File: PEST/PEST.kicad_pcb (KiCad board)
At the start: 4 copper layers, 6.2 x 4.9 mm, 4 parts, among them J1 Conn_01x01, J2 Conn_01x01, J3 Conn_01x01, J4 Conn_01x01

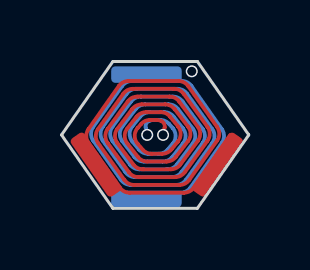
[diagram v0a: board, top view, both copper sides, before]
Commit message: Updated PEST for SMD mounting
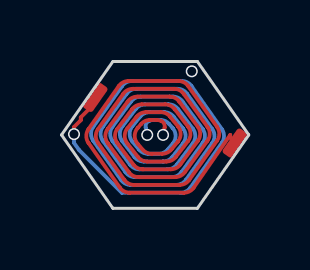
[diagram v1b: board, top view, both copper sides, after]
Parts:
- removed J3, J4: Conn_01x01, PEST:Bridge_Pad
- J2: moved to F.Cu
- moved J2 3.80 mm to (18.0, 18.8), turned to 55 degrees
- moved J1 0.92 mm to (22.7, 20.3)
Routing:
- net Net-(J1-Pin_1): track 195.2 -> 199.7 mm, vias 3 -> 4
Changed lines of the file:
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@@
   (net 1 "Net-(J1-Pin_1)")
   (footprint "PEST:Bridge_Pad" (layer "F.Cu")
-    (at 22.08 20.99 55)
+    (at 22.66 20.27 55)
     (property "Sheetfile" "PEST.kicad_sch")
     (property "Sheetname" "")
@@
         (effects (font (size 1 1) (thickness 0.15)))
     )
-    (fp_text user "${REFERENCE}" (at 0 2.5 55 unlocked) (layer "F.Fab")
-        (effects (font (size 1 1) (thickness 0.15)))
-    )
-    (pad "1" smd roundrect (at 0 0 55) (size 2.35 0.55) (layers "F.Cu" "F.Paste" "F.Mask") (roundrect_rratio 0.25)
+    (pad "1" smd roundrect (at 0 0 55) (size 1 0.4) (layers "F.Cu" "F.Paste" "F.Mask") (roundrect_rratio 0.25)
       (net 1 "Net-(J1-Pin_1)") (pinfunction "Pin_1") (pintype "passive") (thermal_bridge_angle 45))
   )
   (footprint "PEST:Bridge_Pad" (layer "F.Cu")
-    (at 18.03 20.99 -55)
+    (at 18 18.75 55)
     (property "Sheetfile" "PEST.kicad_sch")
     (property "Sheetname" "")
@@
     (property "ki_keywords" "connector")
     (attr smd)
-    (fp_text reference "J3" (at -2.5 -0.5 -55 unlocked) (layer "F.SilkS") hide
+    (fp_text reference "J2" (at -2.5 -0.5 55 unlocked) (layer "F.SilkS") hide
         (effects (font (size 1 1) (thickness 0.1)))
     )
-    (fp_text value "Conn_01x01" (at 0 1 -55 unlocked) (layer "F.Fab")
+    (fp_text value "Conn_01x01" (at 0 1 55 unlocked) (layer "F.Fab")
         (effects (font (size 1 1) (thickness 0.15)))
     )
-    (fp_text user "${REFERENCE}" (at 0 2.5 -55 unlocked) (layer "F.Fab")
+    (fp_text user "${REFERENCE}" (at 0 2.5 55 unlocked) (layer "F.Fab")
         (effects (font (size 1 1) (thickness 0.15)))
     )
-    (pad "1" smd roundrect (at 0 0 305) (size 2.35 0.55) (layers "F.Cu" "F.Paste" "F.Mask") (roundrect_rratio 0.25)
-      (net 1 "Net-(J1-Pin_1)") (pinfunction "Pin_1") (pintype "passive") (thermal_bridge_angle 45))
-  )
-  (footprint "PEST:Bridge_Pad" (layer "B.Cu")
-    (at 19.71 17.99)
-    (property "Sheetfile" "PEST.kicad_sch")
-    (property "Sheetname" "")
-    (property "ki_description" "Generic connector, single row, 01x01, script generated (kicad-library-utils/schlib/autogen/connector/)")
-    (property "ki_keywords" "connector")
-    (attr smd)
-    (fp_text reference "J4" (at -2.5 0.5 180 unlocked) (layer "B.SilkS") hide
-        (effects (font (size 1 1) (thickness 0.1)) (justify mirror))
-    )
-    (fp_text value "Conn_01x01" (at 0 -1 180 unlocked) (layer "B.Fab")
-        (effects (font (size 1 1) (thickness 0.15)) (justify mirror))
-    )
-    (fp_text user "${REFERENCE}" (at 0 -2.5 180 unlocked) (layer "B.Fab")
-        (effects (font (size 1 1) (thickness 0.15)) (justify mirror))
-    )
-    (pad "1" smd roundrect (at 0 0) (size 2.35 0.55) (layers "B.Cu" "B.Paste" "B.Mask") (roundrect_rratio 0.25)
-      (net 1 "Net-(J1-Pin_1)") (pinfunction "Pin_1") (pintype "passive") (thermal_bridge_angle 45))
-  )
-  (footprint "PEST:Bridge_Pad" (layer "B.Cu")
-    (at 19.71 22.14 180)
-    (property "Sheetfile" "PEST.kicad_sch")
-    (property "Sheetname" "")
-    (property "ki_description" "Generic connector, single row, 01x01, script generated (kicad-library-utils/schlib/autogen/connector/)")
-    (property "ki_keywords" "connector")
-    (attr smd)
-    (fp_text reference "J2" (at -2.5 0.5 unlocked) (layer "B.SilkS") hide
-        (effects (font (size 1 1) (thickness 0.1)) (justify mirror))
-    )
-    (fp_text value "Conn_01x01" (at 0 -1 unlocked) (layer "B.Fab")
-        (effects (font (size 1 1) (thickness 0.15)) (justify mirror))
-    )
-    (fp_text user "${REFERENCE}" (at 0 -2.5 unlocked) (layer "B.Fab")
-        (effects (font (size 1 1) (thickness 0.15)) (justify mirror))
-    )
-    (pad "1" smd roundrect (at 0 0 180) (size 2.35 0.55) (layers "B.Cu" "B.Paste" "B.Mask") (roundrect_rratio 0.25)
+    (pad "1" smd roundrect (at 0 0 55) (size 1 0.4) (layers "F.Cu" "F.Paste" "F.Mask") (roundrect_rratio 0.25)
       (net 1 "Net-(J1-Pin_1)") (pinfunction "Pin_1") (pintype "passive") (thermal_bridge_angle 45))
   )
@@
   (segment (start 20.186928 19.242228) (end 19.696407 19.242228) (width 0.127) (layer "F.Cu") (net 1))
   (segment (start 19.740993 20.887676) (end 20.374247 20.887676) (width 0.127) (layer "F.Cu") (net 1))
+  (segment (start 18 18.935845) (end 18 18.75) (width 0.127) (layer "F.Cu") (net 1))
+  (segment (start 22.503 20) (end 22.503 20.083) (width 0.127) (layer "F.Cu") (net 1))
   (segment (start 19.234799 19.141489) (end 18.741901 19.794714) (width 0.127) (layer "F.Cu") (net 1))
   (segment (start 19.884096 20.627868) (end 20.234467 20.627868) (width 0.127) (layer "F.Cu") (net 1))
+  (segment (start 22.503 20.083) (end 22.69 20.27) (width 0.127) (layer "F.Cu") (net 1))
   (segment (start 20.774858 18.202997) (end 19.114606 18.202997) (width 0.127) (layer "F.Cu") (net 1))
   (segment (start 20.69099 20.731958) (end 21.094195 20.209152) (width 0.127) (layer "F.Cu") (net 1))
   (segment (start 20.988534 21.241539) (end 21.742858 20.197439) (width 0.127) (layer "F.Cu") (net 1))
+  (segment (start 17.295147 19.974079) (end 17.295147 19.736968) (width 0.127) (layer "F.Cu") (net 1))
   (segment (start 19.530266 19.639617) (end 19.416309 19.770713) (width 0.127) (layer "F.Cu") (net 1))
   (segment (start 20.760556 19.713911) (end 20.497376 19.389993) (width 0.127) (layer "F.Cu") (net 1))
+  (segment (start 17.295147 19.736968) (end 17.52 19.512115) (width 0.127) (layer "F.Cu") (net 1))
   (segment (start 20.478584 18.722613) (end 19.408912 18.722613) (width 0.127) (layer "F.Cu") (net 1))
   (segment (start 20.046604 19.502035) (end 19.832154 19.502035) (width 0.127) (layer "F.Cu") (net 1))
@@
   (segment (start 19.070581 20.281561) (end 19.426387 20.734704) (width 0.127) (layer "F.Cu") (net 1))
   (segment (start 19.38304 19.39363) (end 19.07182 19.785935) (width 0.127) (layer "F.Cu") (net 1))
+  (segment (start 17.52 19.512115) (end 17.52 19.415845) (width 0.127) (layer "F.Cu") (net 1))
   (segment (start 21.743247 19.729484) (end 20.951045 18.629098) (width 0.127) (layer "F.Cu") (net 1))
   (segment (start 19.150771 21.926907) (end 20.958062 21.926907) (width 0.127) (layer "F.Cu") (net 1))
@@
   (segment (start 18.741181 20.27562) (end 19.274971 20.987458) (width 0.127) (layer "F.Cu") (net 1))
   (segment (start 21.137783 21.498492) (end 22.062894 20.194033) (width 0.127) (layer "F.Cu") (net 1))
+  (segment (start 17.52 19.415845) (end 18 18.935845) (width 0.127) (layer "F.Cu") (net 1))
   (segment (start 18.787523 18.372744) (end 17.777627 19.807337) (width 0.127) (layer "F.Cu") (net 1))
   (segment (start 20.839548 20.985738) (end 21.420589 20.202164) (width 0.127) (layer "F.Cu") (net 1))
@@
   (segment (start 18.096586 20.269351) (end 18.973749 21.499348) (width 0.127) (layer "F.Cu") (net 1))
   (segment (start 19.413709 20.292529) (end 19.579608 20.487266) (width 0.127) (layer "F.Cu") (net 1))
+  (via (at 17.295147 19.974079) (size 0.4) (drill 0.3) (layers "F.Cu" "B.Cu") (net 1))
   (via (at 19.736 20) (size 0.4) (drill 0.3) (layers "F.Cu" "B.Cu") (net 1))
   (via (at 21.22 17.88) (size 0.4) (drill 0.3) (layers "F.Cu" "B.Cu") (net 1))
@@
   (segment (start 19.239444 19.713911) (end 19.502624 19.389993) (width 0.127) (layer "B.Cu") (net 1))
   (segment (start 20.700581 21.667099) (end 19.188495 21.667099) (width 0.127) (layer "B.Cu") (net 1))
+  (segment (start 17.295147 20.263032) (end 17.295147 19.974079) (width 0.127) (layer "B.Cu") (net 1))
   (segment (start 18.862217 21.498492) (end 17.937106 20.194033) (width 0.127) (layer "B.Cu") (net 1))
   (segment (start 20.765201 19.141489) (end 21.258099 19.794714) (width 0.127) (layer "B.Cu") (net 1))
@@
   (segment (start 18.904878 19.721794) (end 19.350558 19.139345) (width 0.127) (layer "B.Cu") (net 1))
   (segment (start 19.521416 18.722612) (end 20.591088 18.722612) (width 0.127) (layer "B.Cu") (net 1))
+  (segment (start 17.462194 20.5016) (end 17.295147 20.263032) (width 0.127) (layer "B.Cu") (net 1))
   (segment (start 20.259007 20.887676) (end 19.625753 20.887676) (width 0.127) (layer "B.Cu") (net 1))
+  (segment (start 18.8875 21.926906) (end 17.462194 20.5016) (width 0.127) (layer "B.Cu") (net 1))
   (segment (start 20.61696 19.39363) (end 20.92818 19.785935) (width 0.127) (layer "B.Cu") (net 1))
   (segment (start 19.373579 18.462805) (end 20.737792 18.462805) (width 0.127) (layer "B.Cu") (net 1))
